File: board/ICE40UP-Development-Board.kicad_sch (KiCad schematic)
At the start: 60 parts, among them X1 USB4105-GF-A, X2 Conn_01x16, X3 Conn_01x16, X4 Tag-Connect, Y1 48MHz

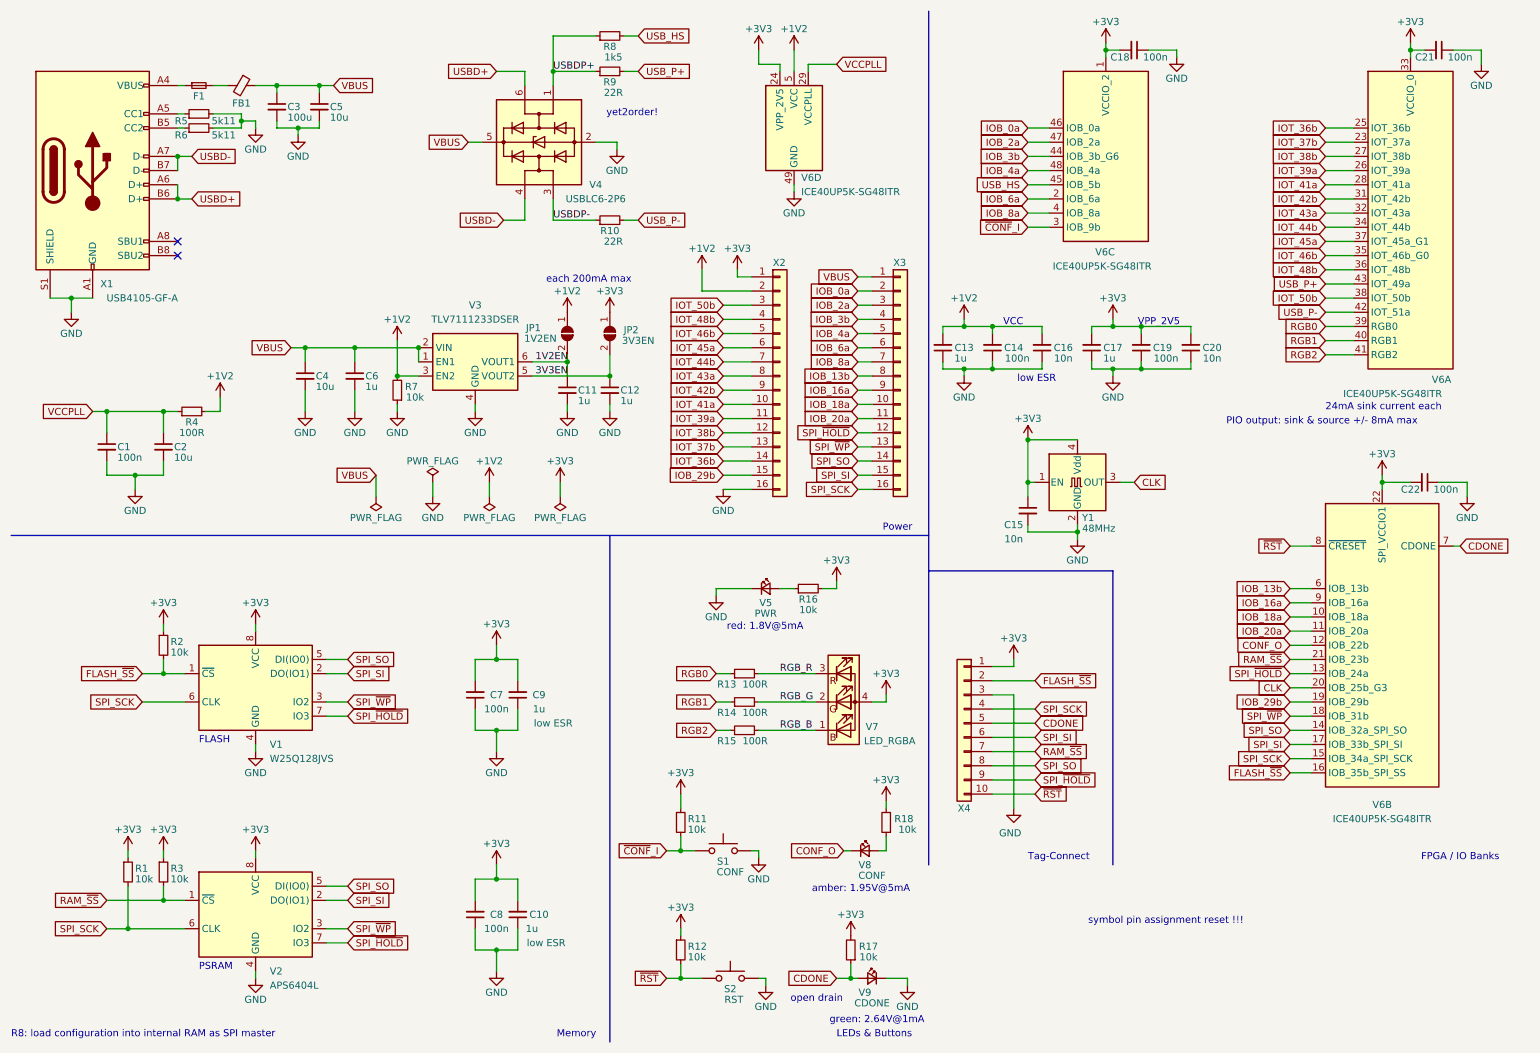
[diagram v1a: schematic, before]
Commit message: change led resistor values, again
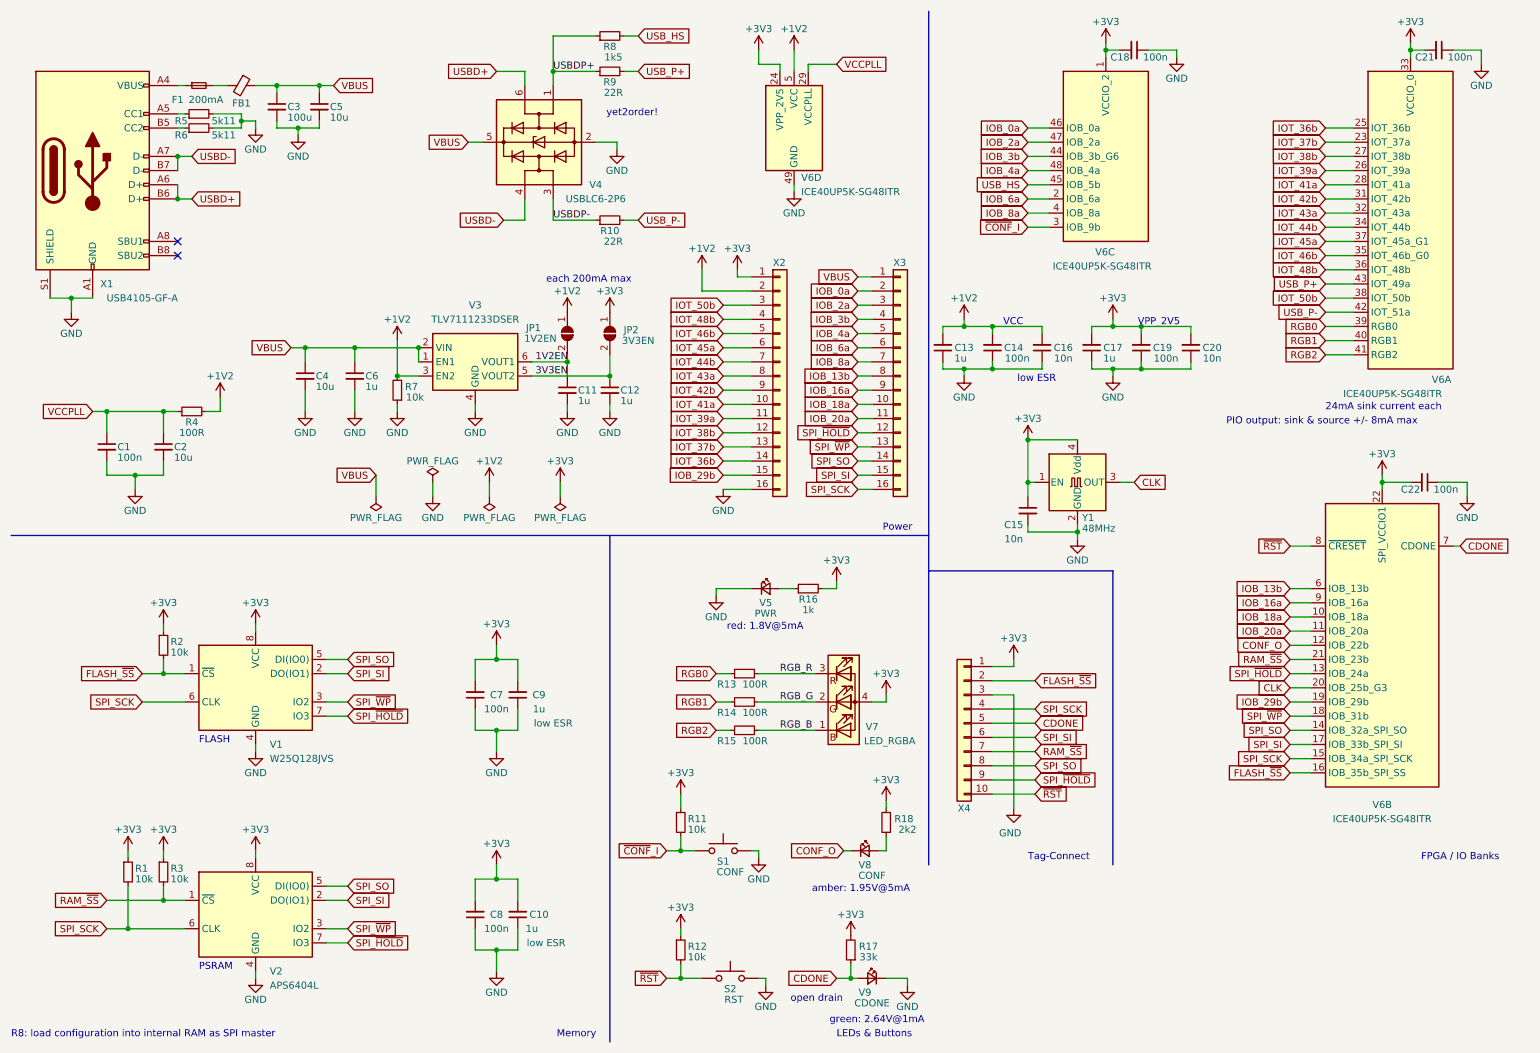
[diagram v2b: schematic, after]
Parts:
- F1: value Fuse_Small -> 200mA
- JP1, JP2: now left out of the parts list
- R16: value 10k -> 1k
- R17: value 10k -> 33k
- R18: value 10k -> 2k2
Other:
- note removed: "symbol pin assignment reset !!!"
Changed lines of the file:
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@@
-    (effects (font (size 1.27 1.27)) (justify left bottom))
-  )
-  (text "symbol pin assignment reset !!!" (at 205.105 177.165 0)
     (effects (font (size 1.27 1.27)) (justify left bottom))
   )
@@
   )
   (symbol (lib_id "Jumper:SolderJumper_2_Open") (at 111.76 71.12 270) (unit 1)
-    (in_bom yes) (on_board yes) (dnp no)
+    (in_bom no) (on_board yes) (dnp no)
     (property "Reference" "JP1" (at 105.664 70.104 90)
       (effects (font (size 1.27 1.27)))
@@
       (effects (font (size 1.27 1.27)))
     )
-    (property "Value" "10k" (at 172.72 160.02 0)
+    (property "Value" "2k2" (at 172.72 160.02 0)
       (effects (font (size 1.27 1.27)))
     )
@@
   (symbol (lib_id "Device:Fuse_Small") (at 45.72 26.67 0) (unit 1)
     (in_bom yes) (on_board yes) (dnp no)
-    (property "Reference" "F1" (at 45.72 28.575 0)
-      (effects (font (size 1.27 1.27)))
-    )
-    (property "Value" "Fuse_Small" (at 45.72 23.495 0)
-      (effects (font (size 1.27 1.27)) hide)
+    (property "Reference" "F1" (at 41.91 29.21 0)
+      (effects (font (size 1.27 1.27)))
+    )
+    (property "Value" "200mA" (at 46.99 29.21 0)
+      (effects (font (size 1.27 1.27)))
     )
     (property "Footprint" "Fuse:Fuse_0805_2012Metric" (at 45.72 26.67 0)
@@
       (effects (font (size 1.27 1.27)))
     )
-    (property "Value" "10k" (at 154.94 120.65 90)
+    (property "Value" "1k" (at 154.94 120.65 90)
       (effects (font (size 1.27 1.27)))
     )
@@
       (effects (font (size 1.27 1.27)))
     )
-    (property "Value" "10k" (at 165.735 182.88 0)
+    (property "Value" "33k" (at 165.735 182.88 0)
       (effects (font (size 1.27 1.27)))
     )
@@
   )
   (symbol (lib_id "Jumper:SolderJumper_2_Open") (at 119.38 71.12 270) (unit 1)
-    (in_bom yes) (on_board yes) (dnp no)
+    (in_bom no) (on_board yes) (dnp no)
     (property "Reference" "JP2" (at 123.19 70.485 90)
       (effects (font (size 1.27 1.27)))

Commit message: update rgb led resistors; change capacitor placement
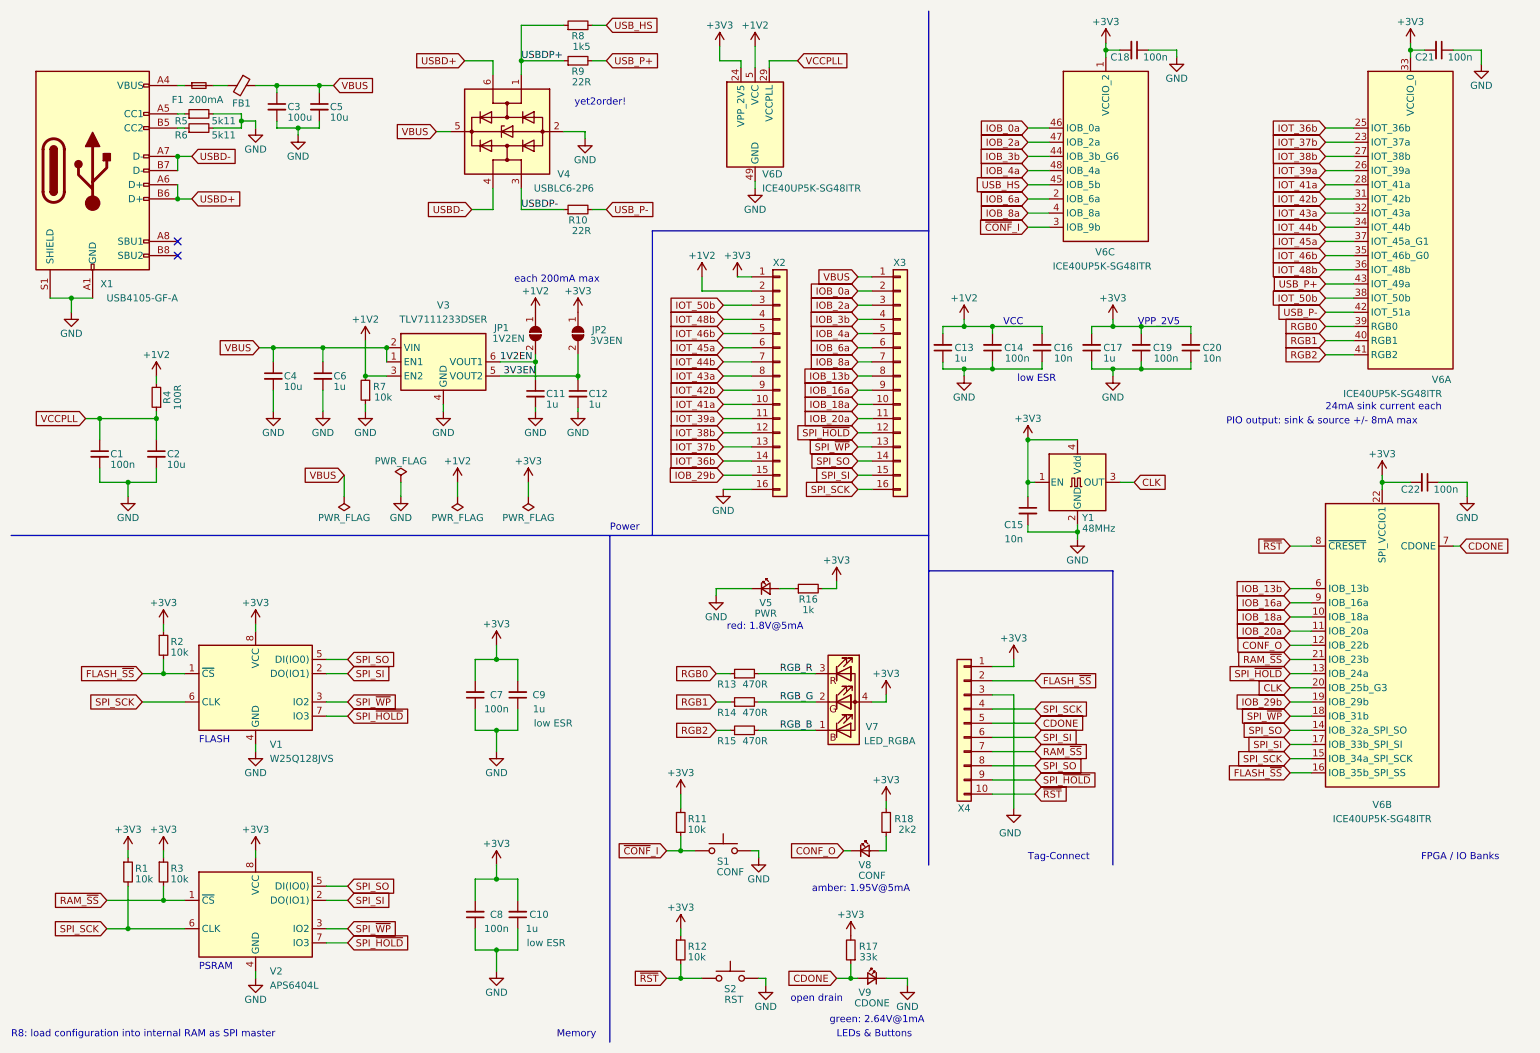
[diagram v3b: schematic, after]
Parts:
- R13, R14, R15: value 100R -> 470R
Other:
- moved on the sheet: C1, C11, C12, C2, C4, C6, JP1, JP2, R10, R4, R7, R8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

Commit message: add QSPI nWP & nHOLD pull-up resistors
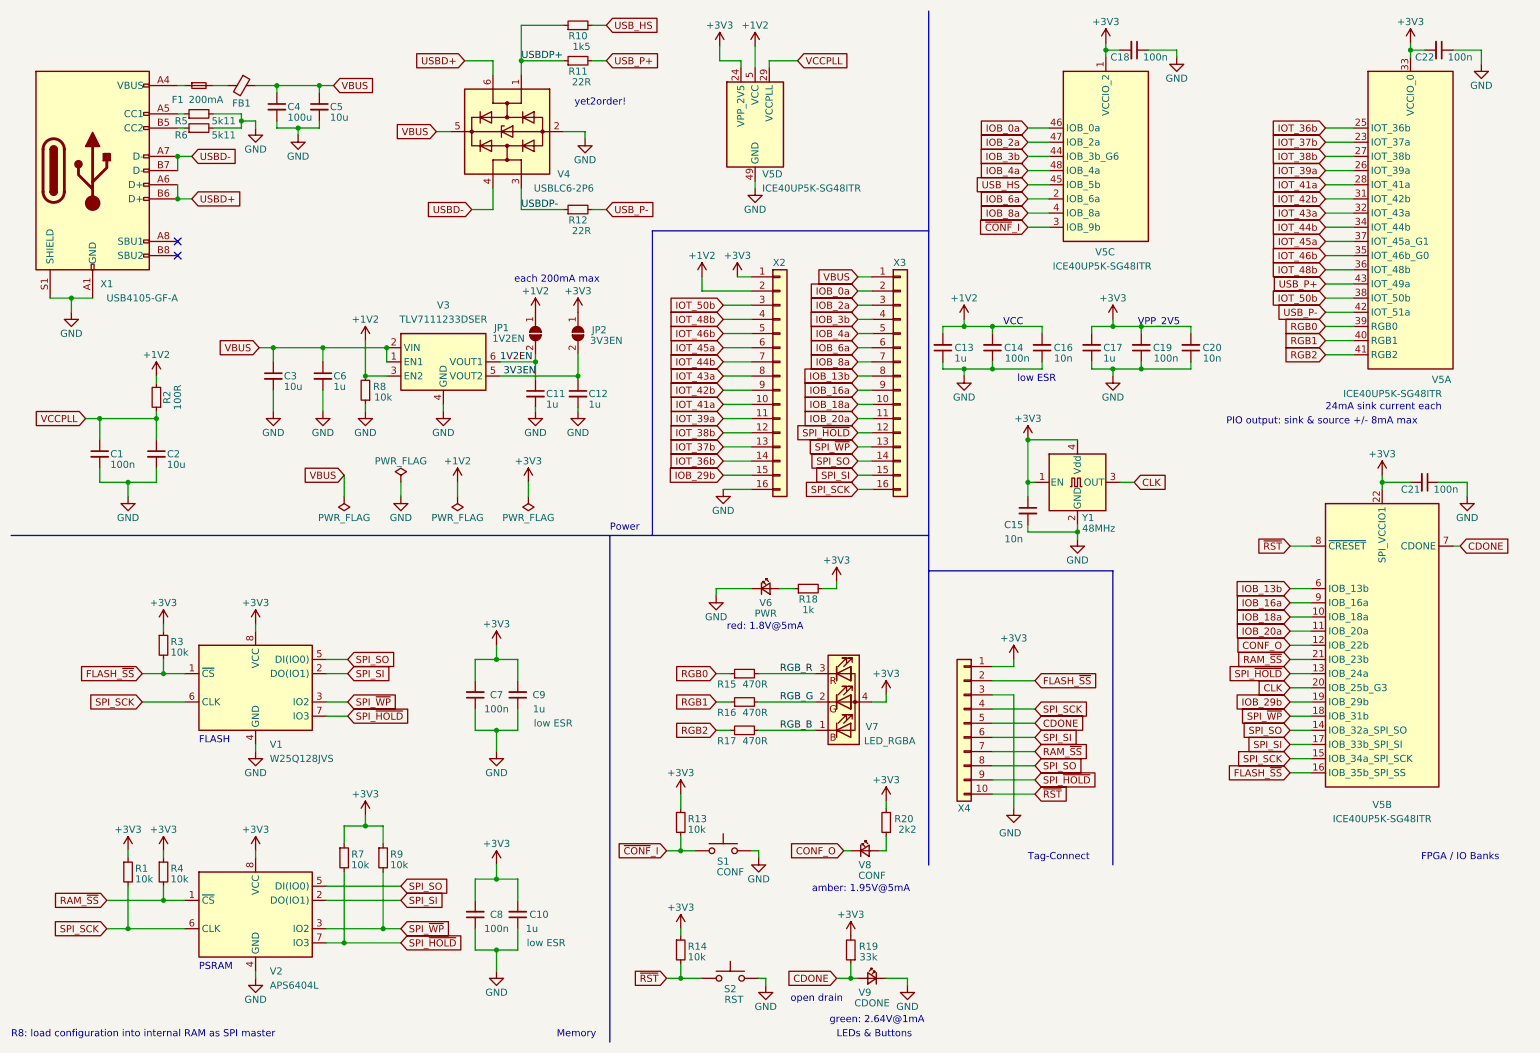
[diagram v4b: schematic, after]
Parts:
- added R7, R9: 10k, Resistor_SMD:R_0402_1005Metric, symbol Device:R_Small
- renumbered C22 to C21, C21 to C22, C4 to C3, C3 to C4, R8 to R10, R9 to R11, R10 to R12, R11 to R13, R12 to R14, R13 to R15, R14 to R16, R15 to R17, R16 to R18, R17 to R19, R4 to R2, R18 to R20, R2 to R3, R3 to R4, R7 to R8, V6 to V5, V5 to V6
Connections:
- net +3V3: now also R7.1, R9.1
- net SPI_~{HOLD}: now also R7.2
- net SPI_~{WP}: now also R9.2
